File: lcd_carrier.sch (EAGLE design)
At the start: 22 parts, among them IC1 MCP2300X/SO, IC2 74LS595D, U1 LCD-16X2SILK

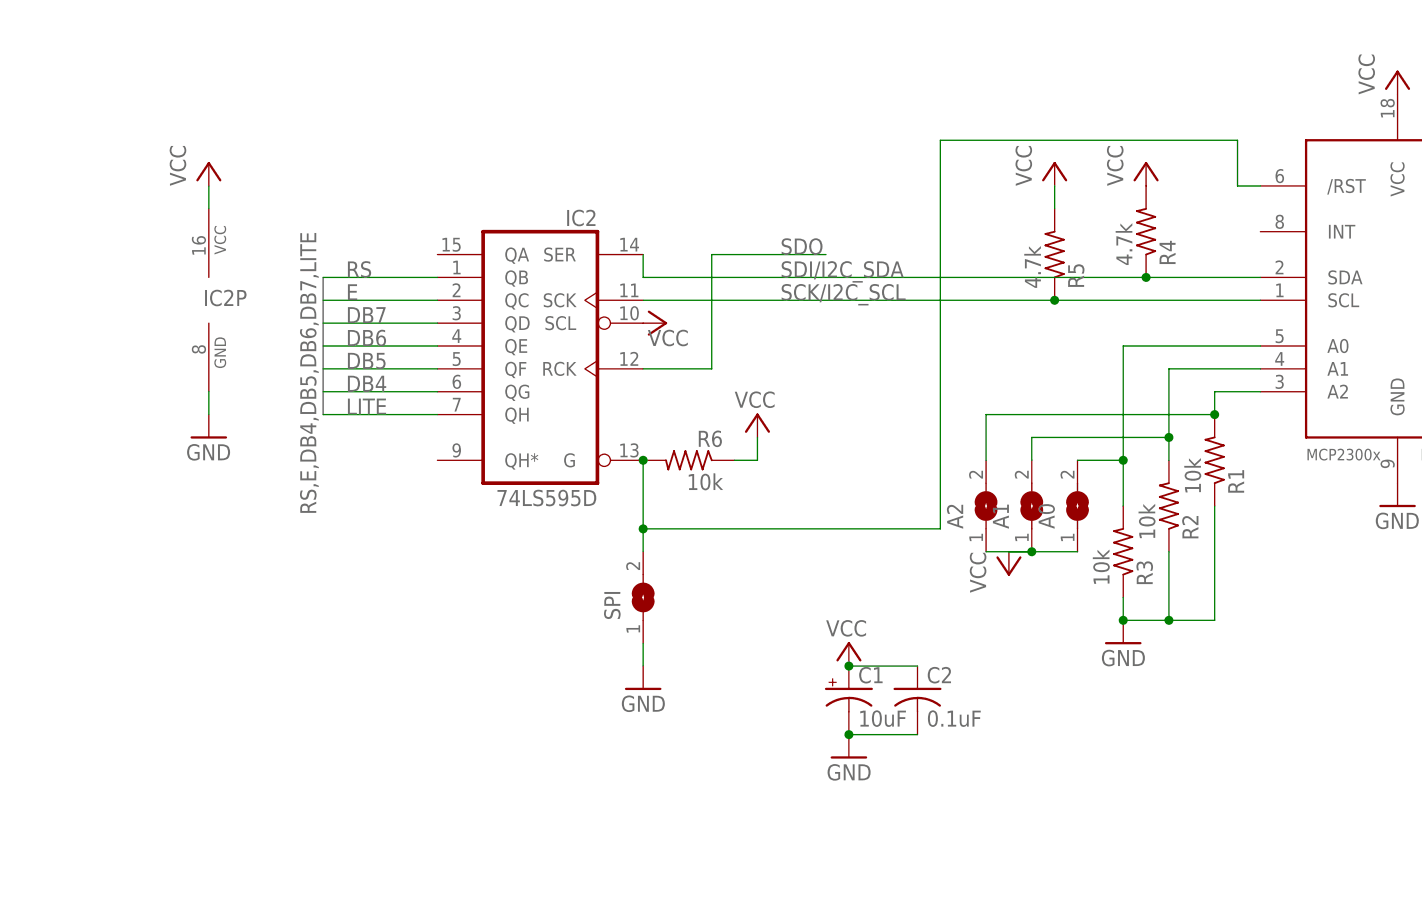
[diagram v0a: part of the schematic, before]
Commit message: Adding LCD carrier board
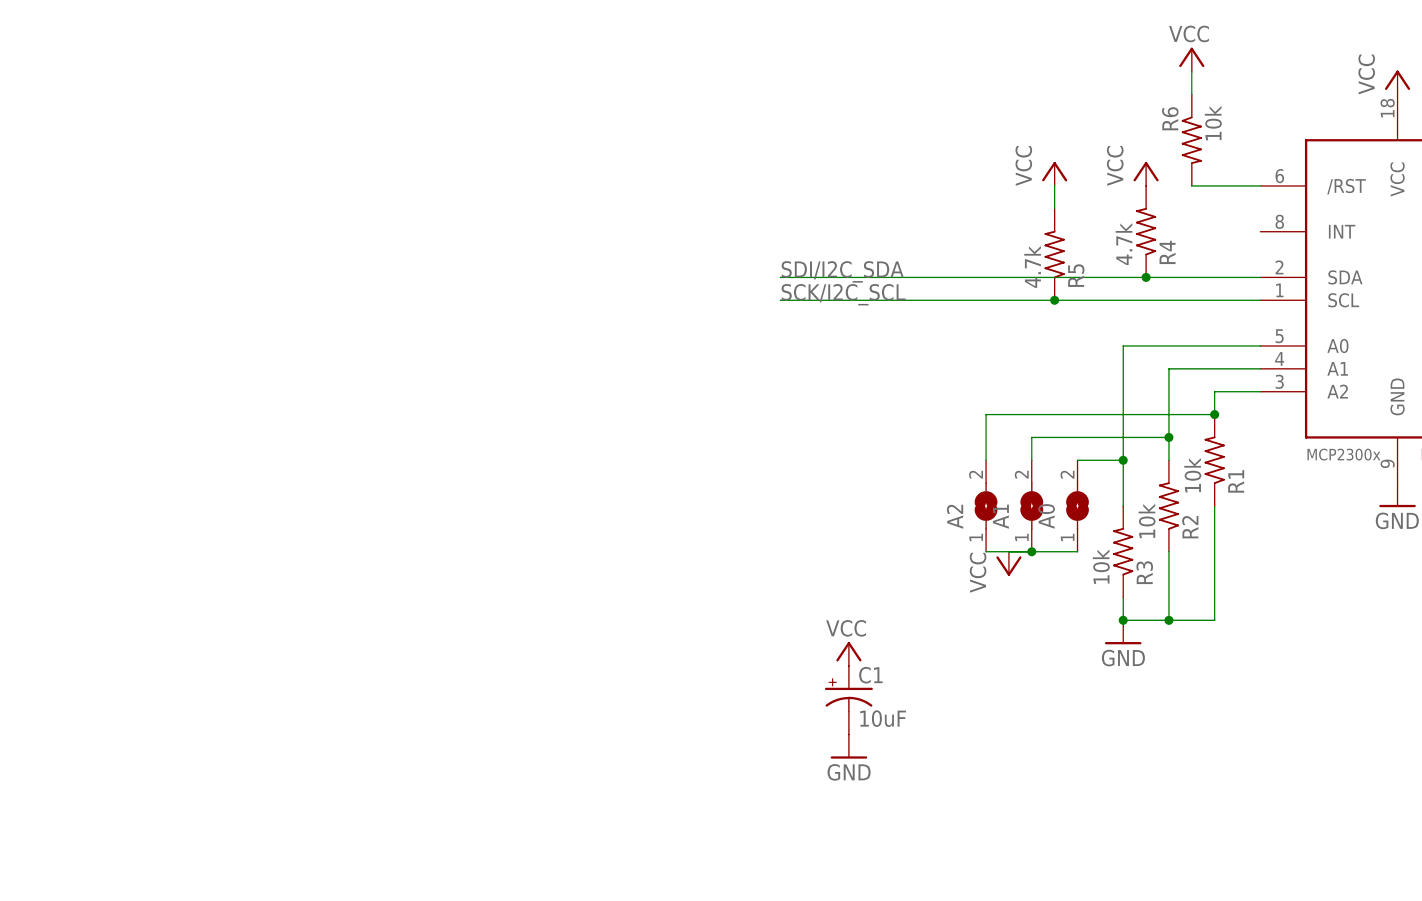
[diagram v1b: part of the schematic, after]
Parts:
- removed C2: 0.1uF, adafruit:C-USC0805K
- removed IC2: 74LS595D, 74xx-us:74LS595D
- removed SPI: (no value), jumper:SJ
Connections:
- removed net N$8: IC1./RST, IC2A.G, R6.2, SPI.2
- new net N$2: IC1./RST, R6.2
- net DB4: no longer IC2A.QG
- net DB5: no longer IC2A.QF
- net DB6: no longer IC2A.QE
- net DB7: no longer IC2A.QD
- net E: no longer IC2A.QC
- net GND: no longer C2.2, IC2P.GND, SPI.1
- net LITE: no longer IC2A.QH
- net RS: no longer IC2A.QB
- net SCK/I2C_SCL: no longer IC2A.SCK
- net SDI/I2C_SDA: no longer IC2A.SER
- net SDO: no longer IC2A.RCK
- net VCC: no longer C2.1, IC2A.SCL, IC2P.VCC
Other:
- moved on the sheet: R6
